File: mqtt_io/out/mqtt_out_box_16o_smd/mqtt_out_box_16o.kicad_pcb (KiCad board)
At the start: 2 copper layers, 135 x 151 mm, 105 parts, among them J1 Conn_01x04_Pin, K1 FINDER-40.31, K10 FINDER-40.31, K11 FINDER-40.31, K12 FINDER-40.31, K13 FINDER-40.31, K14 FINDER-40.31, K15 FINDER-40.31, K16 FINDER-40.31, K2 FINDER-40.31, K3 FINDER-40.31, K4 FINDER-40.31, K5 FINDER-40.31, K6 FINDER-40.31, K7 FINDER-40.31, K8 FINDER-40.31, K9 FINDER-40.31, Q1 IRLML0030, Q10 IRLML0030, Q11 IRLML0030, Q12 IRLML0030, Q13 IRLML0030, Q14 IRLML0030, Q15 IRLML0030, Q16 IRLML0030, Q2 IRLML0030, Q3 IRLML0030, Q4 IRLML0030, Q5 IRLML0030, Q6 IRLML0030, Q7 IRLML0030, Q8 IRLML0030, Q9 IRLML0030, U1 MCP23017_SO

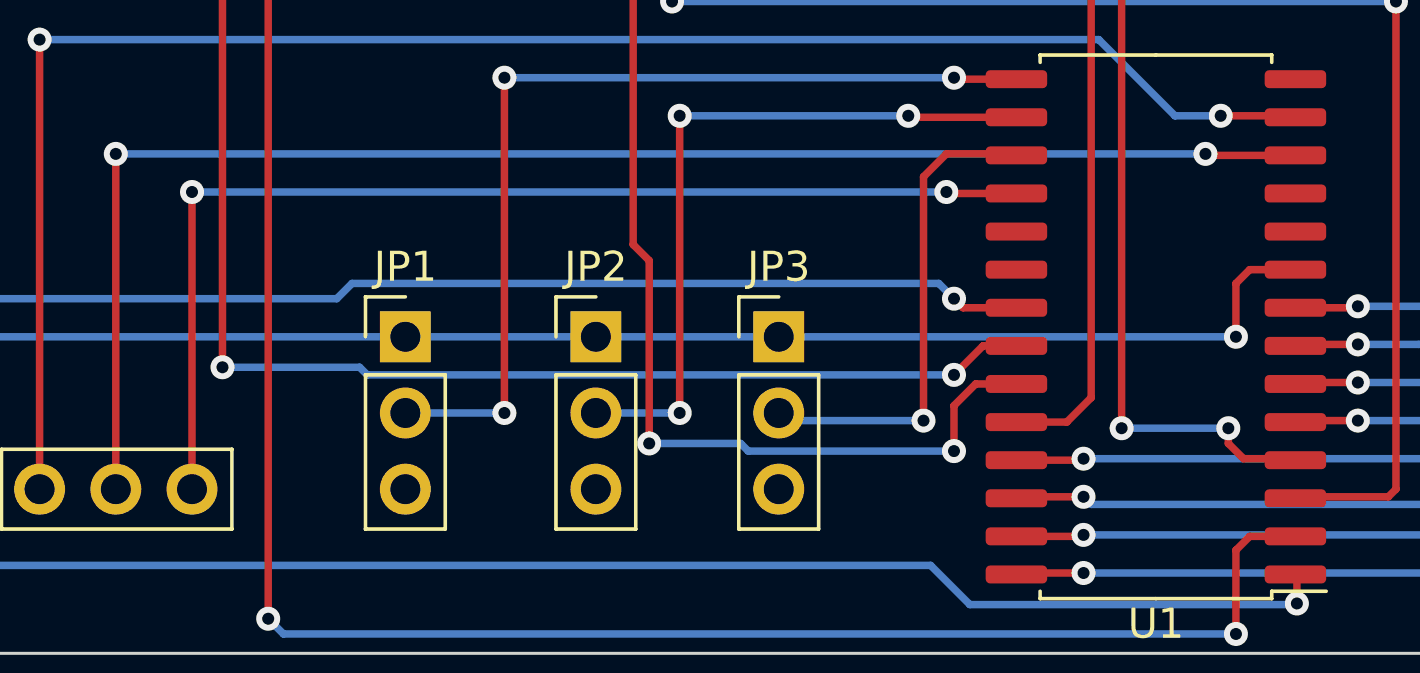
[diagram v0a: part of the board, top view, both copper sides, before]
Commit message: neue Dateien eingefügt.
out Platine rev 2, testprogramm für pi pico
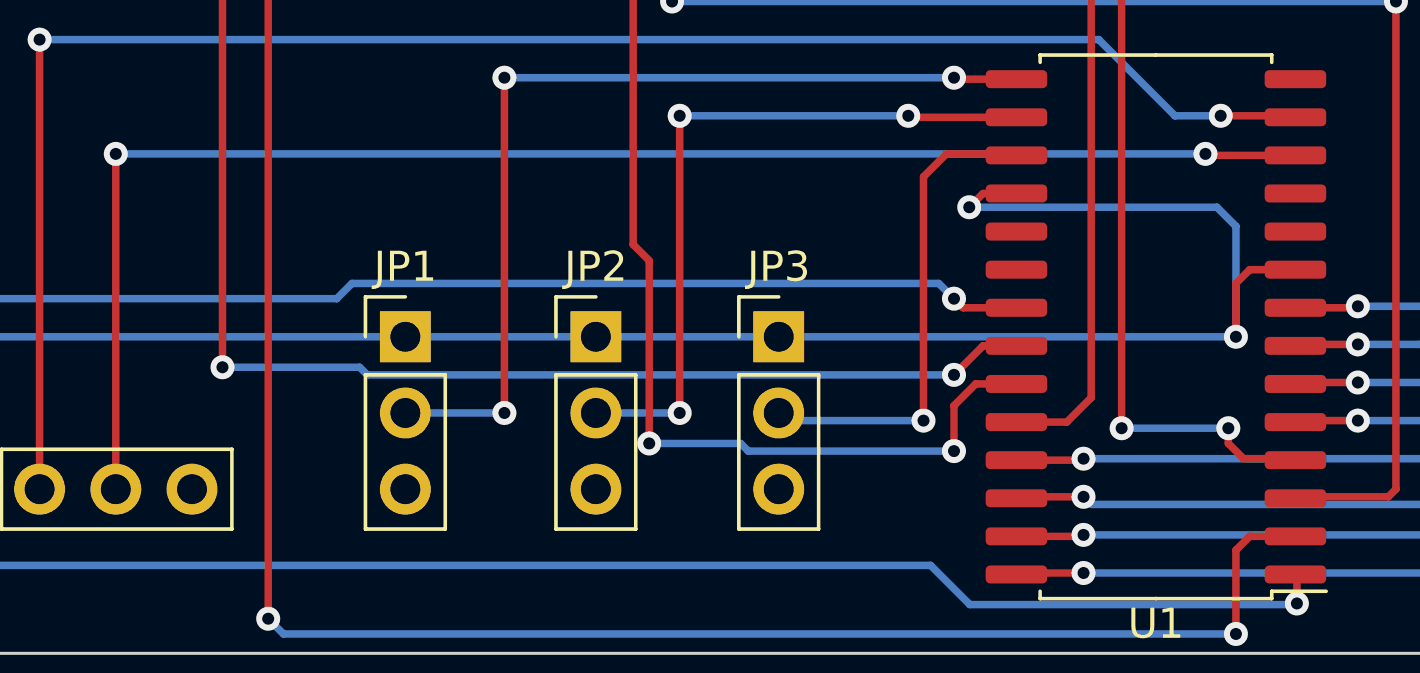
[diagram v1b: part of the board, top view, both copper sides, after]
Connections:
- U1 pad 18: GND -> VCC
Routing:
- net GND: track 37.4 -> 0.00 mm, vias 2 -> 0
- net VCC: track 506.5 -> 521.1 mm, vias 2 -> 3
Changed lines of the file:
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@@
       (net 39 "/AD2") (pinfunction "A2") (pintype "input"))
     (pad "18" smd roundrect (at 4.65 4.445 180) (size 2.05 0.6) (layers "F.Cu" "F.Paste" "F.Mask") (roundrect_rratio 0.25)
-      (net 20 "GND") (pinfunction "~{RESET}") (pintype "input"))
+      (net 1 "VCC") (pinfunction "~{RESET}") (pintype "input"))
     (pad "19" smd roundrect (at 4.65 3.175 180) (size 2.05 0.6) (layers "F.Cu" "F.Paste" "F.Mask") (roundrect_rratio 0.25)
       (net 106 "unconnected-(U1-INTB-Pad19)") (pinfunction "INTB") (pintype "tri_state"))
@@
   (segment (start 41.271714 73.536286) (end 40.132 74.676) (width 0.5) (layer "F.Cu") (net 1))
   (segment (start 126.104 110.624) (end 124.968 111.76) (width 0.5) (layer "F.Cu") (net 1))
+  (segment (start 67.613 150.671) (end 66.499 150.671) (width 0.25) (layer "F.Cu") (net 1))
   (segment (start 111.965284 73.454716) (end 110.744 74.676) (width 0.5) (layer "F.Cu") (net 1))
   (segment (start 111.965284 110.538716) (end 110.744 111.76) (width 0.5) (layer "F.Cu") (net 1))
@@
   (segment (start 126.104 68.26) (end 126.104 73.54) (width 0.5) (layer "F.Cu") (net 1))
   (segment (start 111.965284 105.4) (end 111.965284 110.538716) (width 0.5) (layer "F.Cu") (net 1))
+  (segment (start 66.499 150.671) (end 66.04 151.13) (width 0.25) (layer "F.Cu") (net 1))
   (segment (start 97.82657 68.26) (end 97.82657 73.36943) (width 0.5) (layer "F.Cu") (net 1))
   (segment (start 22.098 78.486) (end 22.098 114.3) (width 1) (layer "F.Cu") (net 1))
@@
   (segment (start 111.965284 68.26) (end 111.965284 73.454716) (width 0.5) (layer "F.Cu") (net 1))
   (via (at 22.098 155.448) (size 0.8) (drill 0.4) (layers "F.Cu" "B.Cu") (net 1))
+  (via (at 66.04 151.13) (size 0.8) (drill 0.4) (layers "F.Cu" "B.Cu") (net 1))
   (via (at 74.93 155.448) (size 0.8) (drill 0.4) (layers "F.Cu" "B.Cu") (net 1))
   (segment (start 52.832 114.046) (end 67.31 114.046) (width 1) (layer "B.Cu") (net 1))
@@
   (segment (start 81.28 114.046) (end 67.31 114.046) (width 1) (layer "B.Cu") (net 1))
   (segment (start 68.072 113.284) (end 67.31 114.046) (width 1) (layer "B.Cu") (net 1))
+  (segment (start 66.04 151.13) (end 74.295 151.13) (width 0.25) (layer "B.Cu") (net 1))
   (segment (start 82.296 111.76) (end 82.296 113.03) (width 1) (layer "B.Cu") (net 1))
   (segment (start 66.6496 77.724) (end 52.578 77.724) (width 1) (layer "B.Cu") (net 1))
@@
   (segment (start 110.744 111.76) (end 110.744 113.284) (width 1) (layer "B.Cu") (net 1))
   (segment (start 109.8296 77.724) (end 95.4024 77.724) (width 1) (layer "B.Cu") (net 1))
+  (segment (start 74.93 151.765) (end 74.93 155.448) (width 0.25) (layer "B.Cu") (net 1))
   (segment (start 124.968 74.676) (end 124.968 76.708) (width 1) (layer "B.Cu") (net 1))
   (segment (start 96.52 113.284) (end 95.758 114.046) (width 1) (layer "B.Cu") (net 1))
@@
   (segment (start 123.952 114.046) (end 109.982 114.046) (width 1) (layer "B.Cu") (net 1))
   (segment (start 124.968 113.03) (end 123.952 114.046) (width 1) (layer "B.Cu") (net 1))
+  (segment (start 74.295 151.13) (end 74.93 151.765) (width 0.25) (layer "B.Cu") (net 1))
   (segment (start 25.908 111.76) (end 25.908 113.03) (width 1) (layer "B.Cu") (net 1))
   (segment (start 53.848 113.03) (end 52.832 114.046) (width 1) (layer "B.Cu") (net 1))
@@
   (via (at 73.914 149.352) (size 0.8) (drill 0.4) (layers "F.Cu" "B.Cu") (net 19))
   (segment (start 73.914 149.352) (end 37.592 149.352) (width 0.25) (layer "B.Cu") (net 19))
-  (segment (start 67.613 150.671) (end 65.327 150.671) (width 0.25) (layer "F.Cu") (net 20))
-  (segment (start 40.132 150.622) (end 40.132 160.528) (width 0.25) (layer "F.Cu") (net 20))
-  (segment (start 65.327 150.671) (end 65.278 150.622) (width 0.25) (layer "F.Cu") (net 20))
-  (via (at 65.278 150.622) (size 0.8) (drill 0.4) (layers "F.Cu" "B.Cu") (net 20))
-  (via (at 40.132 150.622) (size 0.8) (drill 0.4) (layers "F.Cu" "B.Cu") (net 20))
-  (segment (start 65.278 150.622) (end 40.132 150.622) (width 0.25) (layer "B.Cu") (net 20))
   (segment (start 29.544 25.4292) (end 29.6672 25.5524) (width 0.5) (layer "F.Cu") (net 21))
   (segment (start 29.544 18.368) (end 29.544 23.368) (width 0.5) (layer "F.Cu") (net 21))
